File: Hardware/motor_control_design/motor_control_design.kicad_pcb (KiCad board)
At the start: 2 copper layers, 57.1 x 57.2 mm, 83 parts, among them J10 3V3, J2 SWD, J3 VBAT, J4 GND, J5 FC_M/P, J6 Conn_01x06, J8 Conn_01x06, J9 GND, Q1 RF1S9540SM, Q10 2N7002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

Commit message: Motor Board: Added LCSC Part Numbers Fixed missing ground on diode
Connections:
- net /PWR_LED_K renamed Net-(D1-K)
- D11 pad 2: unconnected-(D11-A-Pad2) -> GND
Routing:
- net GND: track 194.5 -> 197.0 mm, vias 22 -> 23

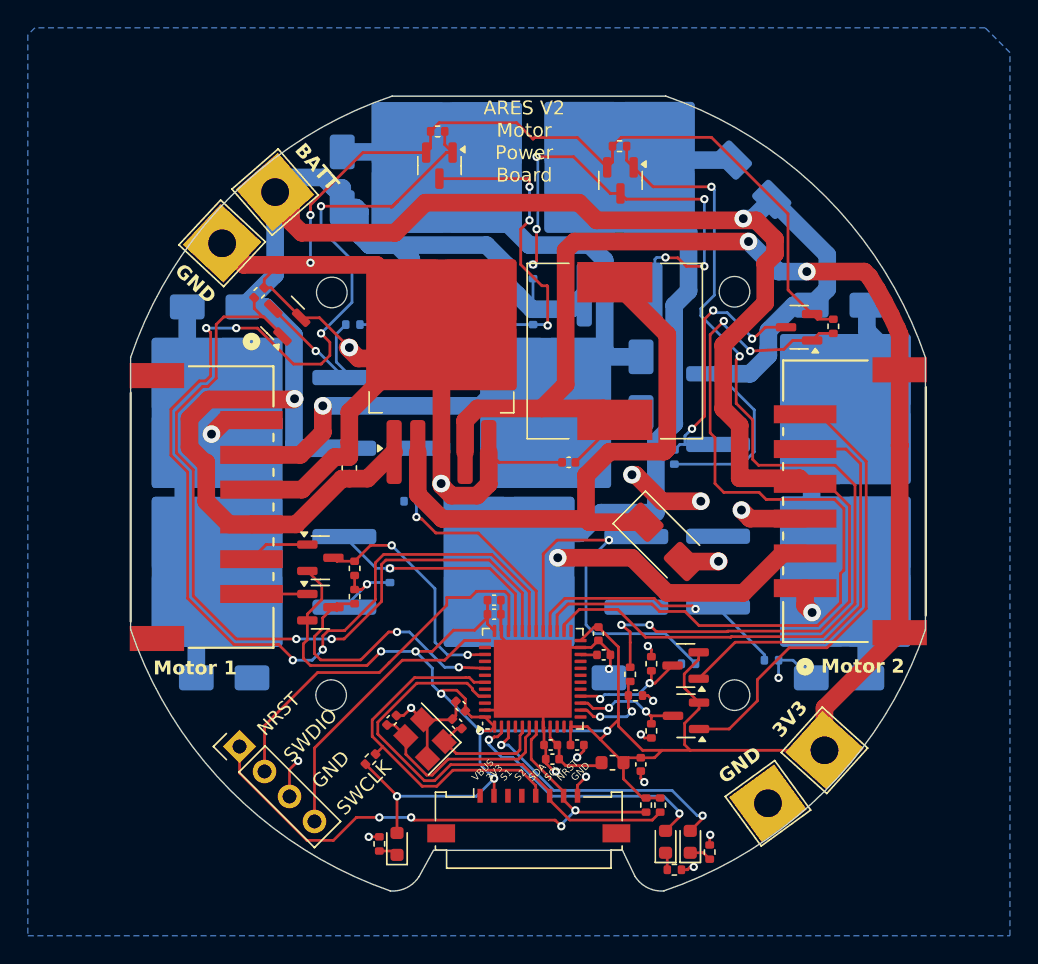
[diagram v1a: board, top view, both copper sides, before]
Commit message: Motor Board: Optimized LM2576 circuit - bigger capacitor - better inductor Added assembly files (outdated)
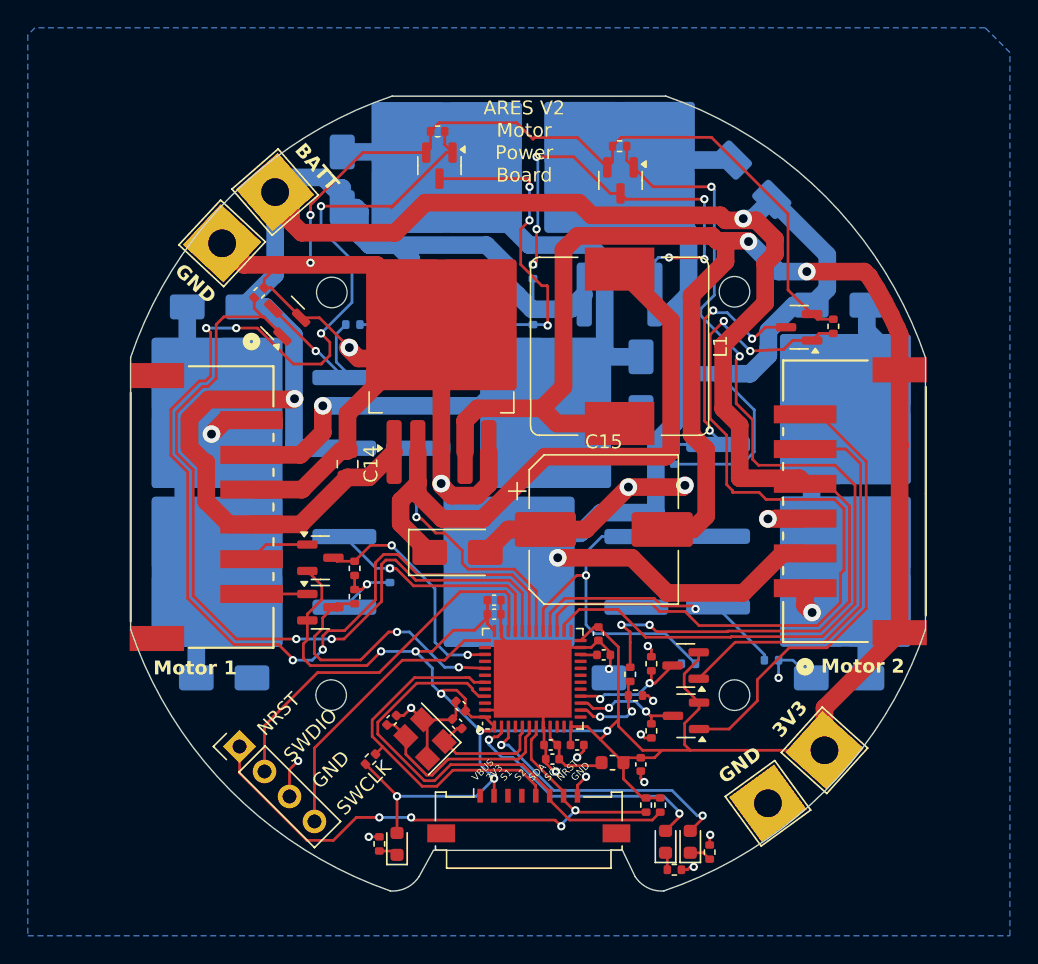
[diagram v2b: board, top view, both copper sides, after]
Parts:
- C14: footprint Capacitor_SMD:C_0603_1608Metric -> Capacitor_SMD:C_0805_2012Metric
- C15: value 330uF -> 1000uF; footprint Capacitor_SMD:C_0402_1005Metric -> Capacitor_SMD:CP_Elec_10x10.5
- L1: footprint Inductor_SMD:L_12x12mm_H4.5mm -> Inductor_SMD:L_TaiTech_TMPC1265_13.5x12.5mm
- moved D11 14.8 mm to (143.9, 93.3), turned to 0 degrees
- moved C15 5.44 mm to (154.4, 91.7)
- moved L1 0.48 mm to (155.6, 78.5)
- moved C14 0.30 mm to (136.0, 87.0)
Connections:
- J8 pad 7: +3.3V -> (no net)
- J8 pad 8: +3.3V -> (no net)
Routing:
- net +3.3V: track 206.1 -> 227.8 mm
- net /M2Q4: track 26.5 -> 24.0 mm
- net Net-(D11-K): track 43.4 -> 45.1 mm
- net /M1Q4: track 18.8 -> 19.3 mm
- net GND: vias 23 -> 22

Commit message: Added Via Stiching and ViPs to Motor Board
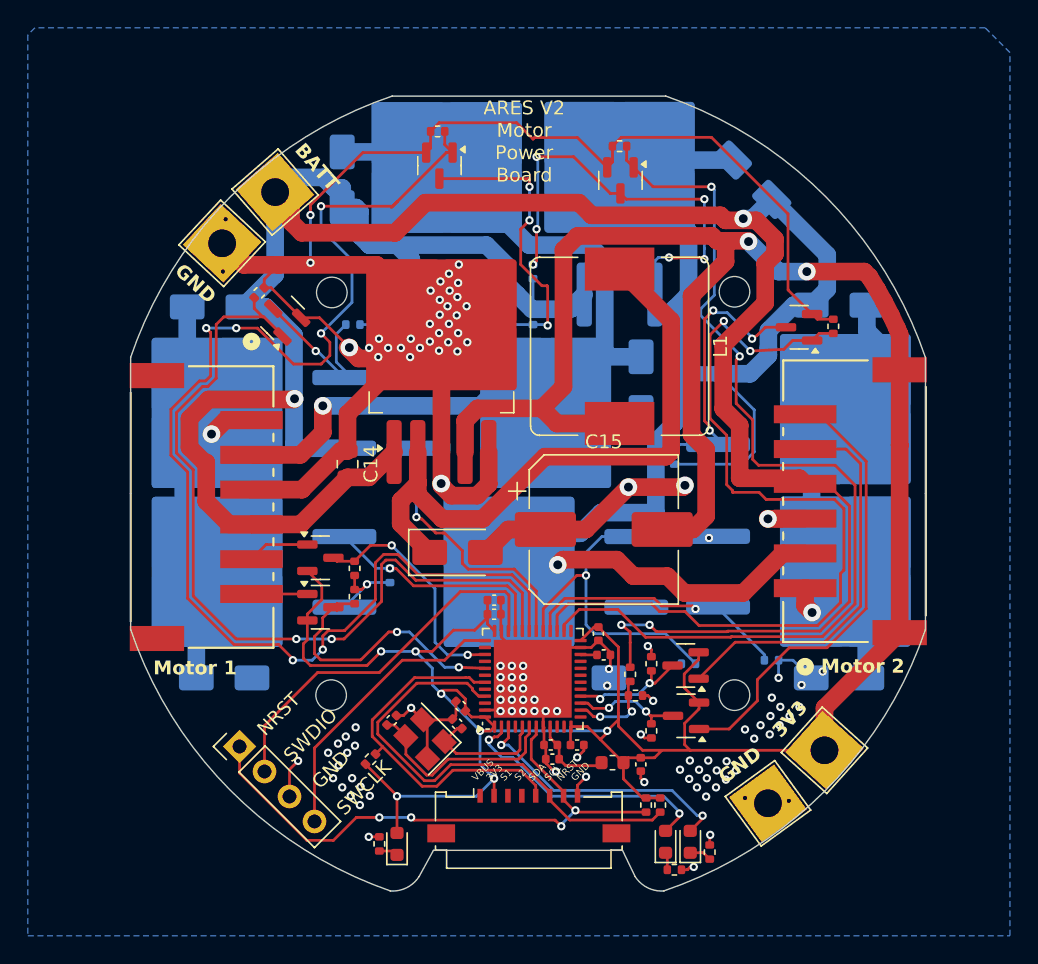
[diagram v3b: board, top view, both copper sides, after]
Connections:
- J8 pad 7: (no net) -> +3.3V
- J8 pad 8: (no net) -> +3.3V
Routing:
- net GND: track 197.0 -> 197.1 mm, vias 22 -> 115
